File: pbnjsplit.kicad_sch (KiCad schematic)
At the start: 3 parts

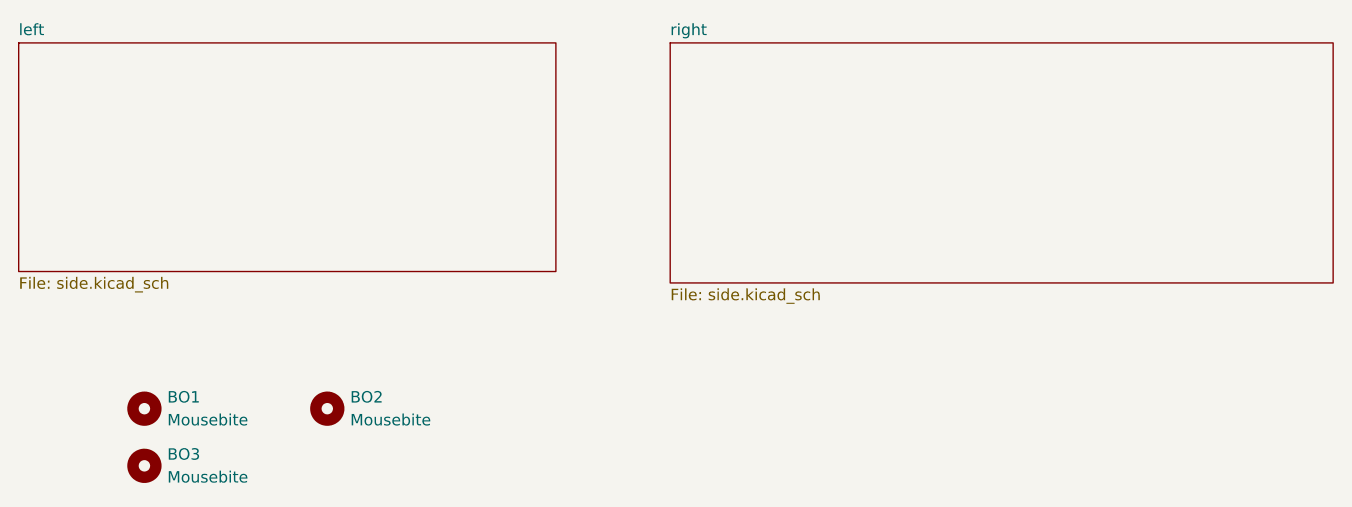
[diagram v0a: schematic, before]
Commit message: add LEDs
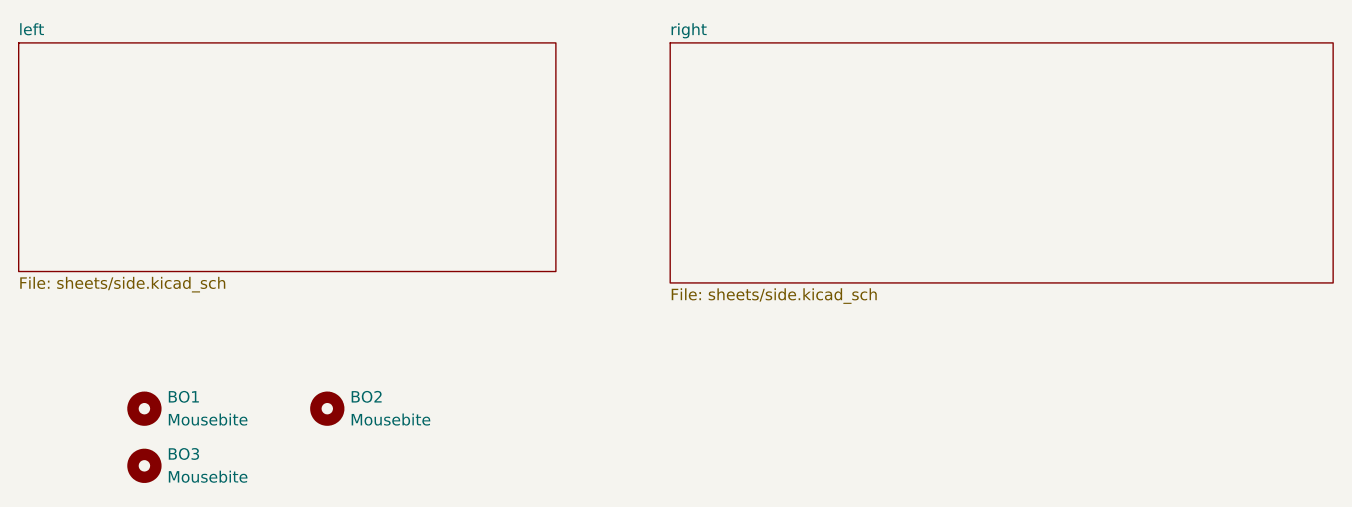
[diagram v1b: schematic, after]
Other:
- sheet left: file side.kicad_sch -> sheets/side.kicad_sch
- sheet right: file side.kicad_sch -> sheets/side.kicad_sch
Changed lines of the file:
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@@
 			)
 		)
-		(property "Sheetfile" "side.kicad_sch"
+		(property "Sheetfile" "sheets/side.kicad_sch"
 			(at 33.02 56.4646 0)
 			(show_name no)
@@
 			)
 		)
-		(property "Sheetfile" "side.kicad_sch"
+		(property "Sheetfile" "sheets/side.kicad_sch"
 			(at 105.41 57.7346 0)
 			(show_name no)
